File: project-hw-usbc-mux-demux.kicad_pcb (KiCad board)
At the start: 4 copper layers, 23 parts, among them J1 Amphenol_12402012E212A, J2 Amphenol_12402012E212A, J3 Amphenol_12402012E212A, J4 Conn_01x04_Pin, Q1 Q_Toshiba_SSM3J328R, Q2 Q_Toshiba_SSM3J328R, U1 LMR516x5, U2 FUSB303BTMX

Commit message: pcb: route most of the board
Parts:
- TP1: footprint TestPoint:TestPoint_Pad_D2.0mm -> TestPoint:TestPoint_Pad_D1.0mm
- moved TP1 93.2 mm to (63.0, 36.5)
- moved U2 87.7 mm to (58.0, 40.0), turned to 180 degrees
- moved R5 84.6 mm to (55.0, 47.0), turned to -90 degrees
- moved Q2 83.4 mm to (56.5, 36.0), turned to -90 degrees
- moved R6 82.9 mm to (53.5, 47.0), turned to -90 degrees
- moved R4 81.2 mm to (59.5, 36.0), turned to -90 degrees
- moved R7 79.2 mm to (50.0, 45.0), turned to -90 degrees
- moved D1 79.2 mm to (50.0, 48.0), turned to 90 degrees
- moved Q1 78.3 mm to (52.5, 36.0), turned to -90 degrees
- moved D2 77.1 mm to (52.5, 31.5)
- moved R3 74.6 mm to (52.5, 33.0)
- moved J4 36.7 mm to (53.8, 22.0), turned to -90 degrees
- moved C1 4.12 mm to (42.0, 46.0)
- moved C2 4.12 mm to (39.0, 39.5)
- moved C3 4.12 mm to (35.0, 46.5)
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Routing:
- net /D-: track 0.00 -> 48.1 mm, vias 0 -> 2
- net /D+: track 0.00 -> 46.5 mm, vias 0 -> 2
- net Net-(J1-CC2): track 0.00 -> 31.9 mm, vias 0 -> 2
- net Net-(J1-CC1): track 0.00 -> 26.7 mm, vias 0 -> 2
- net GND: track 0.00 -> 13.4 mm, vias 12 -> 18
- net Net-(D2-K): track 0.00 -> 8.12 mm
- net /ID: track 0.00 -> 6.98 mm, vias 0 -> 2
- net Net-(D1-A): track 0.00 -> 1.39 mm
- net +5V: vias 2 -> 12
- added copper zone on In1.Cu, net +5V
- added copper zone on F.Cu, net /Load Switch/Out
- added copper zone on In2.Cu, net GND
- added copper zone on F.Cu, net Net-(D2-A)
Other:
- board outline added: 40 x 30 mm

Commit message: pcb: first draft ready
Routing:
- net +5V: track 16.9 -> 26.7 mm, vias 12 -> 14
- net Net-(U2-SDA/OUT1): track 0.00 -> 8.62 mm, vias 0 -> 2
- net Net-(J3-CC1): track 0.00 -> 7.83 mm, vias 0 -> 2
- net Net-(U2-SCL/OUT2): track 0.00 -> 7.31 mm, vias 0 -> 2
- net Net-(J3-CC2): track 0.00 -> 6.10 mm, vias 0 -> 2
- net Net-(U2-PORT/~{DEBUG}): track 0.00 -> 5.63 mm, vias 0 -> 2
- net /Load Switch/Out: track 0.00 -> 2.81 mm
- net /ID: track 6.98 -> 9.19 mm
- added copper zone on In1.Cu, net GND

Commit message: pcb: add silkscreen
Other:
- board text added: "5V"
- board text added: "Common"
- board text added: "Data"
- board text added: "GND"
- board text added: "PD"
- board text added: "VBUS PD"

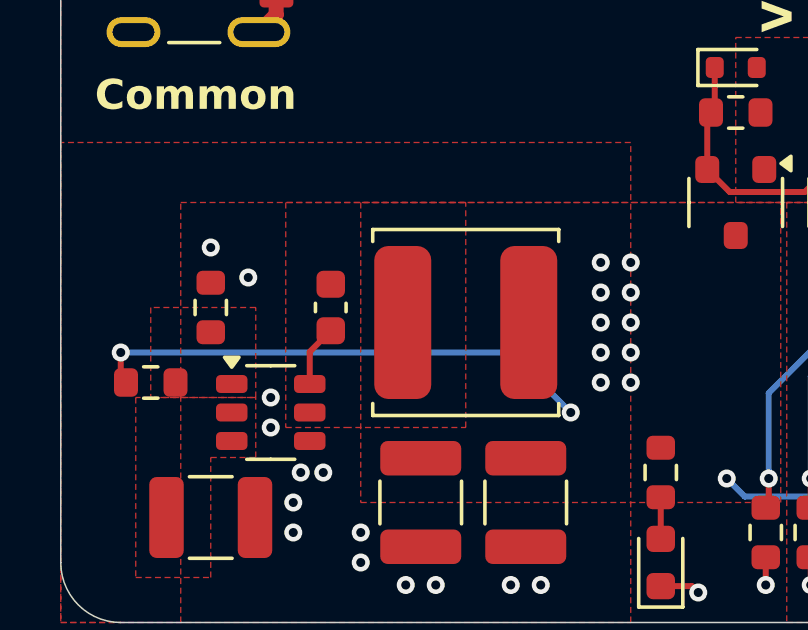
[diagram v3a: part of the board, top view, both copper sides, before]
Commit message: pcb: make pd poor wider
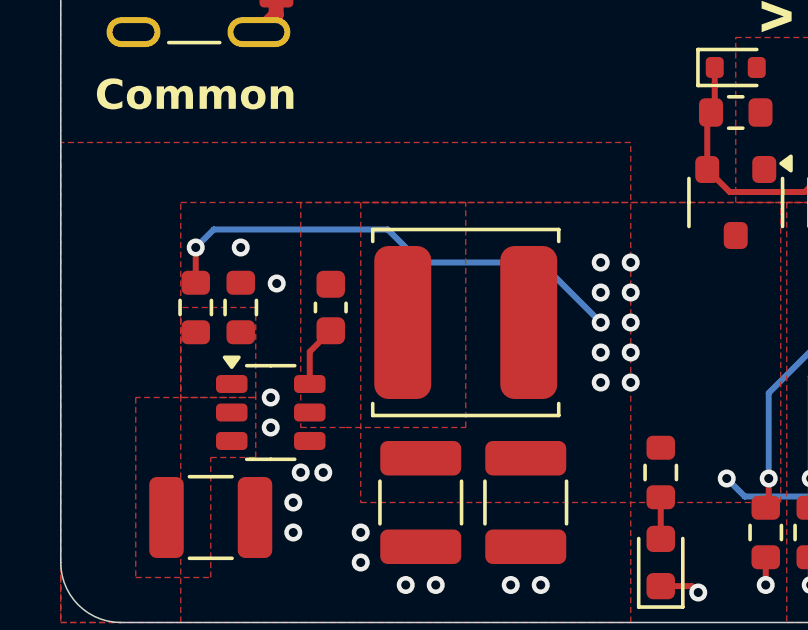
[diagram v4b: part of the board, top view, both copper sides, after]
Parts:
- moved R1 2.92 mm to (34.5, 39.5), turned to -90 degrees
- moved R2 1.00 mm to (36.0, 39.5)
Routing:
- net +5V: track 26.7 -> 26.0 mm, vias 14 -> 13
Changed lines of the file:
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@@
 	(footprint "Resistor_SMD:R_0603_1608Metric"
 		(layer "F.Cu")
-		(at 33 42)
+		(at 34.5 39.5 -90)
 		(descr "Resistor SMD 0603 (1608 Metric), square (rectangular) end terminal, IPC_7351 nominal, (Body size source: IPC-SM-782 page 72, https://www.pcb-3d.com/wordpress/wp-content/uploads/ipc-sm-782a_amendment_1_and_2.pdf), generated with kicad-footprint-generator")
 		(tags "resistor")
 		(property "Reference" "R1"
-			(at 0 -1.43 0)
+			(at 0 -1.43 90)
 			(layer "F.SilkS")
 			(hide yes)
@@
 		)
 		(property "Value" "52.3k"
-			(at 0 1.43 0)
+			(at 0 1.43 90)
 			(layer "F.Fab")
 			(effects
@@
 		)
 		(property "Footprint" "Resistor_SMD:R_0603_1608Metric"
-			(at 0 0 0)
+			(at 0 0 -90)
 			(unlocked yes)
 			(layer "F.Fab")
@@
 		)
 		(property "Datasheet" ""
-			(at 0 0 0)
+			(at 0 0 -90)
 			(unlocked yes)
 			(layer "F.Fab")
@@
 		)
 		(property "Description" "Resistor, small symbol"
-			(at 0 0 0)
+			(at 0 0 -90)
 			(unlocked yes)
 			(layer "F.Fab")
@@
 		(attr smd)
 		(fp_line
-			(start -0.237258 -0.5225)
-			(end 0.237258 -0.5225)
+			(start -0.237258 0.5225)
+			(end 0.237258 0.5225)
 			(stroke
 				(width 0.12)
@@
 		)
 		(fp_line
-			(start -0.237258 0.5225)
-			(end 0.237258 0.5225)
+			(start -0.237258 -0.5225)
+			(end 0.237258 -0.5225)
 			(stroke
 				(width 0.12)
@@
 		)
 		(fp_line
-			(start -1.48 -0.73)
-			(end 1.48 -0.73)
+			(start -1.48 0.73)
+			(end -1.48 -0.73)
 			(stroke
 				(width 0.05)
@@
 		)
 		(fp_line
-			(start -1.48 0.73)
-			(end -1.48 -0.73)
+			(start 1.48 0.73)
+			(end -1.48 0.73)
 			(stroke
 				(width 0.05)
@@
 		)
 		(fp_line
-			(start 1.48 -0.73)
-			(end 1.48 0.73)
+			(start -1.48 -0.73)
+			(end 1.48 -0.73)
 			(stroke
 				(width 0.05)
@@
 		)
 		(fp_line
-			(start 1.48 0.73)
-			(end -1.48 0.73)
+			(start 1.48 -0.73)
+			(end 1.48 0.73)
 			(stroke
 				(width 0.05)
@@
 		)
 		(fp_line
-			(start -0.8 -0.4125)
-			(end 0.8 -0.4125)
+			(start -0.8 0.4125)
+			(end -0.8 -0.4125)
 			(stroke
 				(width 0.1)
@@
 		)
 		(fp_line
-			(start -0.8 0.4125)
-			(end -0.8 -0.4125)
+			(start 0.8 0.4125)
+			(end -0.8 0.4125)
 			(stroke
 				(width 0.1)
@@
 		)
 		(fp_line
-			(start 0.8 -0.4125)
-			(end 0.8 0.4125)
+			(start -0.8 -0.4125)
+			(end 0.8 -0.4125)
 			(stroke
 				(width 0.1)
@@
 		)
 		(fp_line
-			(start 0.8 0.4125)
-			(end -0.8 0.4125)
+			(start 0.8 -0.4125)
+			(end 0.8 0.4125)
 			(stroke
 				(width 0.1)
@@
 		)
 		(fp_text user "${REFERENCE}"
-			(at 0 0 0)
+			(at 0 0 90)
 			(layer "F.Fab")
 			(effects
@@
 		)
 		(pad "1" smd roundrect
-			(at -0.825 0)
+			(at -0.825 0 270)
 			(size 0.8 0.95)
 			(layers "F.Cu" "F.Paste" "F.Mask")
@@
 		)
 		(pad "2" smd roundrect
-			(at 0.825 0)
+			(at 0.825 0 270)
 			(size 0.8 0.95)
 			(layers "F.Cu" "F.Paste" "F.Mask")
@@
 	(footprint "Resistor_SMD:R_0603_1608Metric"
 		(layer "F.Cu")
-		(at 35 39.5 90)
+		(at 36 39.5 90)
 		(descr "Resistor SMD 0603 (1608 Metric), square (rectangular) end terminal, IPC_7351 nominal, (Body size source: IPC-SM-782 page 72, https://www.pcb-3d.com/wordpress/wp-content/uploads/ipc-sm-782a_amendment_1_and_2.pdf), generated with kicad-footprint-generator")
 		(tags "resistor")
@@
 	)
 	(via
+		(at 37.2 38.7)
+		(size 0.6)
+		(drill 0.3)
+		(layers "F.Cu" "B.Cu")
+		(free yes)
+		(net 1)
+	)
+	(via
 		(at 51.25 49)
 		(size 0.6)
@@
 	)
 	(via
-		(at 35 37.5)
+		(at 36 37.5)
 		(size 0.6)
 		(drill 0.3)
@@
 	)
 	(via
-		(at 36.25 38.5)
-		(size 0.6)
-		(drill 0.3)
-		(layers "F.Cu" "B.Cu")
-		(free yes)
-		(net 1)
-	)
-	(via
 		(at 53.5 48.75)
 		(size 0.6)
@@
 	)
 	(segment
-		(start 32.175 42)
-		(end 32 41.825)
-		(width 0.2)
-		(layer "F.Cu")
-		(net 2)
-	)
-	(segment
-		(start 32 41.825)
-		(end 32 41)
+		(start 34.5 38.675)
+		(end 34.5 37.5)
 		(width 0.2)
 		(layer "F.Cu")
@@
 	)
 	(via
+		(at 34.5 37.5)
+		(size 0.6)
+		(drill 0.3)
+		(layers "F.Cu" "B.Cu")
+		(net 2)
+	)
+	(via
 		(at 48 39)
 		(size 0.6)
@@
 	)
 	(via
-		(at 47 43)
-		(size 0.6)
-		(drill 0.3)
-		(layers "F.Cu" "B.Cu")
-		(net 2)
-	)
-	(via
 		(at 48 41)
 		(size 0.6)
@@
 	)
 	(via
-		(at 32 41)
-		(size 0.6)
-		(drill 0.3)
-		(layers "F.Cu" "B.Cu")
-		(net 2)
-	)
-	(via
 		(at 48 40)
 		(size 0.6)
@@
 	)
 	(segment
-		(start 32 41)
-		(end 45 41)
+		(start 46 38)
+		(end 48 40)
 		(width 0.2)
 		(layer "B.Cu")
@@
 	)
 	(segment
-		(start 45 41)
-		(end 47 43)
+		(start 40.9 36.9)
+		(end 42 38)
+		(width 0.2)
+		(layer "B.Cu")
+		(net 2)
+	)
+	(segment
+		(start 35.1 36.9)
+		(end 40.9 36.9)
+		(width 0.2)
+		(layer "B.Cu")
+		(net 2)
+	)
+	(segment
+		(start 34.5 37.5)
+		(end 35.1 36.9)
+		(width 0.2)
+		(layer "B.Cu")
+		(net 2)
+	)
+	(segment
+		(start 42 38)
+		(end 46 38)
 		(width 0.2)
 		(layer "B.Cu")
@@
 		(polygon
 			(pts
-				(xy 33 42.5) (xy 36.5 42.5) (xy 36.5 39.5) (xy 33 39.5)
+				(xy 34 42.5) (xy 36.5 42.5) (xy 36.5 39.5) (xy 34 39.5)
 			)
 		)
@@
 		(polygon
 			(pts
-				(xy 37.5 43.5) (xy 39.5 43.5) (xy 39.5 43.5) (xy 43.5 43.5) (xy 43.5 36) (xy 37.5 36)
+				(xy 38 43.5) (xy 39.5 43.5) (xy 39.5 43.5) (xy 43.5 43.5) (xy 43.5 36) (xy 38 36)
 			)
 		)

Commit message: pcb: add version
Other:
- board text added: "v1.0.0"
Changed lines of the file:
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@@
 		(layer "Edge.Cuts")
+	)
+	(gr_text "v1.0.0"
+		(at 38 49.5 0)
+		(layer "B.SilkS")
+		(effects
+			(font
+				(face "FreeSans")
+				(size 1.5 1.5)
+				(thickness 0.1)
+			)
+			(justify left bottom mirror)
+		)
+		(render_cache "v1.0.0" 0
+			(polygon
+				(pts
+					(xy 37.398429 49.245) (xy 37.590771 49.245) (xy 37.97875 48.142976) (xy 37.780547 48.142976) (xy 37.485258 49.036905)
+					(xy 37.172749 48.142976) (xy 36.974546 48.142976)
+				)
+			)
+			(polygon
+				(pts
+					(xy 36.412909 48.166423) (xy 36.744103 48.166423) (xy 36.744103 48.025739) (xy 36.668712 48.015289)
+					(xy 36.594039 48.001339) (xy 36.519052 47.980622) (xy 36.463468 47.953932) (xy 36.413026 47.897253)
+					(xy 36.378093 47.827158) (xy 36.352568 47.754492) (xy 36.349528 47.744371) (xy 36.227163 47.744371)
+					(xy 36.227163 49.245) (xy 36.412909 49.245)
+				)
+			)
+			(polygon
+				(pts
+					(xy 35.404675 49.033974) (xy 35.404675 49.245) (xy 35.624127 49.245) (xy 35.624127 49.033974)
+				)
+			)
+			(polygon
+				(pts
+					(xy 34.747572 47.747597) (xy 34.819958 47.761224) (xy 34.88758 47.788643) (xy 34.949651 47.828635)
+					(xy 34.97026 47.845072) (xy 35.023114 47.899087) (xy 35.065788 47.959794) (xy 35.068794 47.964892)
+					(xy 35.10236 48.03556) (xy 35.126789 48.107831) (xy 35.146022 48.183276) (xy 35.149837 48.201308)
+					(xy 35.162637 48.27687) (xy 35.171498 48.357929) (xy 35.176021 48.433362) (xy 35.177529 48.513004)
+					(xy 35.177408 48.53664) (xy 35.174488 48.627627) (xy 35.167676 48.712924) (xy 35.156971 48.792531)
+					(xy 35.142374 48.866448) (xy 35.118653 48.950842) (xy 35.08885 49.026346) (xy 35.052965 49.092958)
+					(xy 35.036943 49.117048) (xy 34.983448 49.179993) (xy 34.921813 49.22895) (xy 34.852037 49.263919)
+					(xy 34.774122 49.2849) (xy 34.688066 49.291894) (xy 34.658696 49.291126) (xy 34.57589 49.279598)
+					(xy 34.501045 49.254237) (xy 34.434159 49.215043) (xy 34.375233 49.162017) (xy 34.324267 49.095157)
+					(xy 34.316536 49.082666) (xy 34.281561 49.015073) (xy 34.252722 48.938911) (xy 34.23002 48.85418)
+					(xy 34.216275 48.780226) (xy 34.206458 48.700788) (xy 34.200567 48.615866) (xy 34.198604 48.52546)
+					(xy 34.198945 48.508607) (xy 34.388381 48.508607) (xy 34.389537 48.585246) (xy 34.394234 48.673767)
+					(xy 34.402546 48.754203) (xy 34.41447 48.826553) (xy 34.43355 48.902699) (xy 34.462386 48.976821)
+					(xy 34.492912 49.028118) (xy 34.549616 49.085163) (xy 34.619419 49.118329) (xy 34.692463 49.127763)
+					(xy 34.777532 49.112799) (xy 34.848182 49.067907) (xy 34.894321 49.010445) (xy 34.931232 48.933829)
+					(xy 34.95286 48.863797) (xy 34.969297 48.782991) (xy 34.980543 48.691411) (xy 34.986599 48.589057)
+					(xy 34.987752 48.514836) (xy 34.98746 48.477532) (xy 34.98307 48.372726) (xy 34.973412 48.278579)
+					(xy 34.958486 48.19509) (xy 34.930391 48.10035) (xy 34.89293 48.024559) (xy 34.846104 47.967715)
+					(xy 34.774402 47.923306) (xy 34.688066 47.908503) (xy 34.651776 47.910847) (xy 34.571294 47.937219)
+					(xy 34.505445 47.992892) (xy 34.463302 48.058529) (xy 34.430524 48.142919) (xy 34.412086 48.218518)
+					(xy 34.398916 48.304665) (xy 34.391014 48.401362) (xy 34.388381 48.508607) (xy 34.198945 48.508607)
+					(xy 34.200516 48.430875) (xy 34.206252 48.342392) (xy 34.215811 48.260012) (xy 34.229195 48.183734)
+					(xy 34.256441 48.080758) (xy 34.29229 47.991513) (xy 34.336743 47.915997) (xy 34.3898 47.854212)
+					(xy 34.451461 47.806157) (xy 34.521726 47.771832) (xy 34.600594 47.751236) (xy 34.688066 47.744371)
+				)
+			)
+			(polygon
+				(pts
+					(xy 33.713538 49.033974) (xy 33.713538 49.245) (xy 33.93299 49.245) (xy 33.93299 49.033974)
+				)
+			)
+			(polygon
+				(pts
+					(xy 33.056435 47.747597) (xy 33.12882 47.761224) (xy 33.196442 47.788643) (xy 33.258513 47.828635)
+					(xy 33.279123 47.845072) (xy 33.331977 47.899087) (xy 33.374651 47.959794) (xy 33.377657 47.964892)
+					(xy 33.411222 48.03556) (xy 33.435651 48.107831) (xy 33.454884 48.183276) (xy 33.4587 48.201308)
+					(xy 33.4715 48.27687) (xy 33.480361 48.357929) (xy 33.484884 48.433362) (xy 33.486392 48.513004)
+					(xy 33.48627 48.53664) (xy 33.483351 48.627627) (xy 33.476538 48.712924) (xy 33.465834 48.792531)
+					(xy 33.451236 48.866448) (xy 33.427516 48.950842) (xy 33.397713 49.026346) (xy 33.361828 49.092958)
+					(xy 33.345805 49.117048) (xy 33.29231 49.179993) (xy 33.230675 49.22895) (xy 33.1609 49.263919)
+					(xy 33.082985 49.2849) (xy 32.996929 49.291894) (xy 32.967558 49.291126) (xy 32.884753 49.279598)
+					(xy 32.809907 49.254237) (xy 32.743021 49.215043) (xy 32.684095 49.162017) (xy 32.633129 49.095157)
+					(xy 32.625398 49.082666) (xy 32.590424 49.015073) (xy 32.561585 48.938911) (xy 32.538882 48.85418)
+					(xy 32.525138 48.780226) (xy 32.51532 48.700788) (xy 32.50943 48.615866) (xy 32.507466 48.52546)
+					(xy 32.507807 48.508607) (xy 32.697243 48.508607) (xy 32.698399 48.585246) (xy 32.703097 48.673767)
+					(xy 32.711408 48.754203) (xy 32.723333 48.826553) (xy 32.742412 48.902699) (xy 32.771249 48.976821)
+					(xy 32.801774 49.028118) (xy 32.858478 49.085163) (xy 32.928282 49.118329) (xy 33.001325 49.127763)
+					(xy 33.086394 49.112799) (xy 33.157045 49.067907) (xy 33.203184 49.010445) (xy 33.240095 48.933829)
+					(xy 33.261722 48.863797) (xy 33.278159 48.782991) (xy 33.289406 48.691411) (xy 33.295462 48.589057)
+					(xy 33.296615 48.514836) (xy 33.296322 48.477532) (xy 33.291932 48.372726) (xy 33.282275 48.278579)
+					(xy 33.267349 48.19509) (xy 33.239253 48.10035) (xy 33.201792 48.024559) (xy 33.154967 47.967715)
+					(xy 33.083264 47.923306) (xy 32.996929 47.908503) (xy 32.960639 47.910847) (xy 32.880157 47.937219)
+					(xy 32.814308 47.992892) (xy 32.772165 48.058529) (xy 32.739386 48.142919) (xy 32.720949 48.218518)
+					(xy 32.707779 48.304665) (xy 32.699877 48.401362) (xy 32.697243 48.508607) (xy 32.507807 48.508607)
+					(xy 32.509378 48.430875) (xy 32.515114 48.342392) (xy 32.524674 48.260012) (xy 32.538058 48.183734)
+					(xy 32.565303 48.080758) (xy 32.601153 47.991513) (xy 32.645606 47.915997) (xy 32.698663 47.854212)
+					(xy 32.760324 47.806157) (xy 32.830588 47.771832) (xy 32.909457 47.751236) (xy 32.996929 47.744371)
+				)
+			)
+		)
 	)
 	(gr_text "PD"

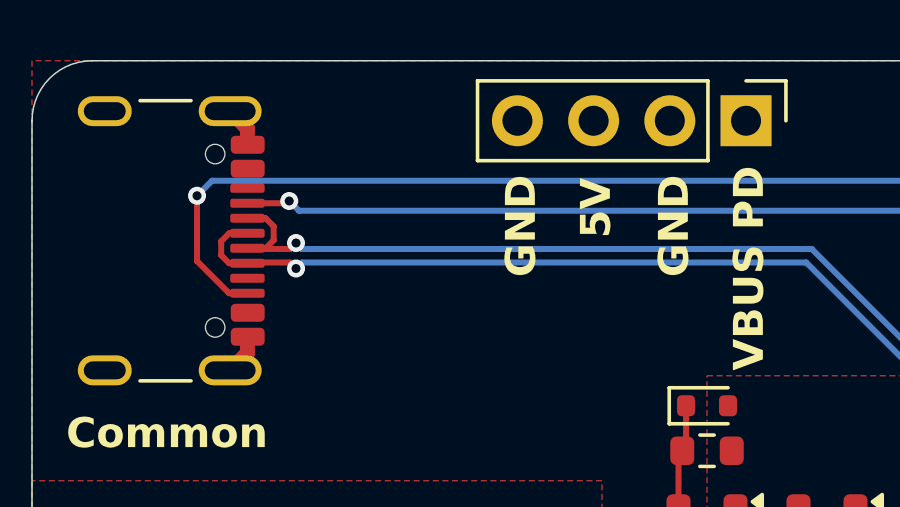
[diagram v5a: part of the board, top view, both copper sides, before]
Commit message: pcb: add dragon logo
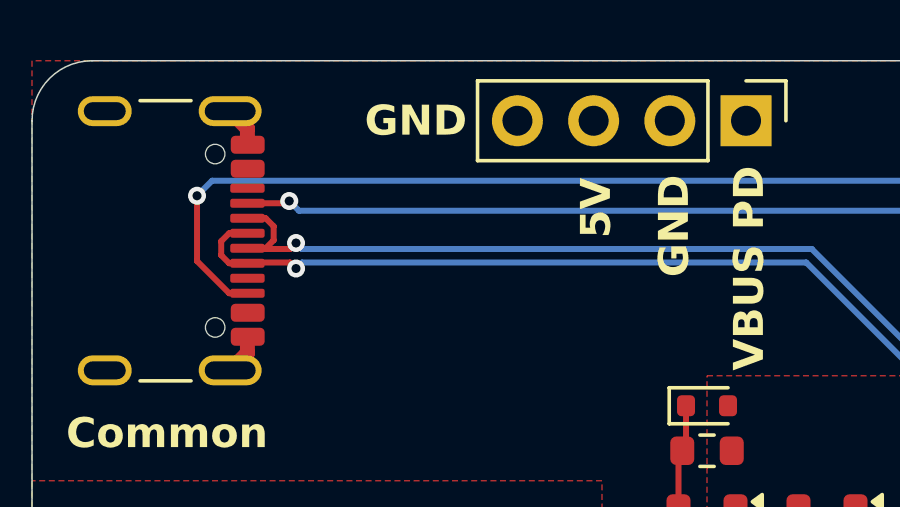
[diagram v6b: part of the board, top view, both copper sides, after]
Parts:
- added G***: LOGO, logos:dragon_16mm, F.Cu at (44.5, 29.0)
